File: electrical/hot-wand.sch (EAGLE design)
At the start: 186 parts, among them IC1 12V R-78K12-2.0, IC2 3V3 R-78K3.3, Q1 STP19NF20, Q2 IRF510, Q3 BC846B, Q4 SIRS5800DP-T1-GE3, Q5 2N7002K, Q6 DMTH64M2LPDWQ-13, Q7 G3404, SW1 SW-TACT-SIDE, U1 TPS54560DDA, U2 1EDN8511BXUSA1, U3 INA138, U4 LM74700QDBVTQ1, U5 AP53781, U6 SSD1306-4PIN-0.91N-VERT, U7 STM32F030F4P6, Y1 27.12 MHz 10pF

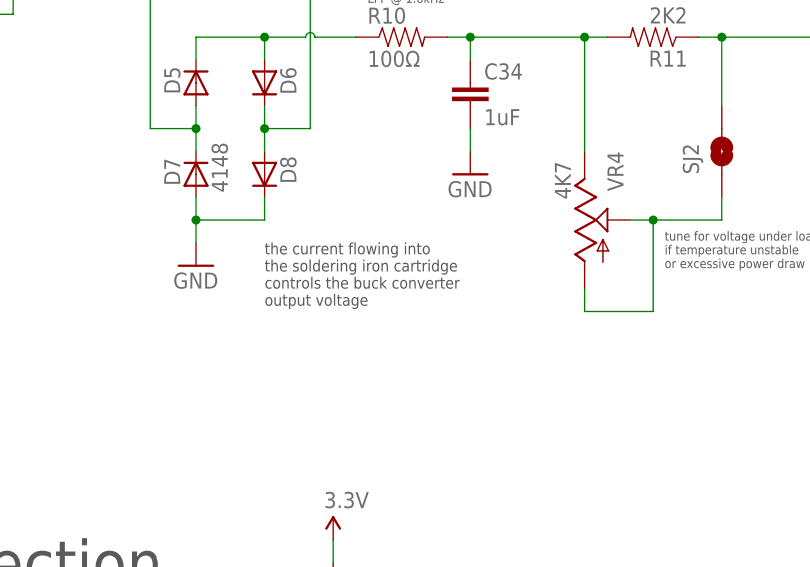
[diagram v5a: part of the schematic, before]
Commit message: 22 ohm resistor now 2W capable
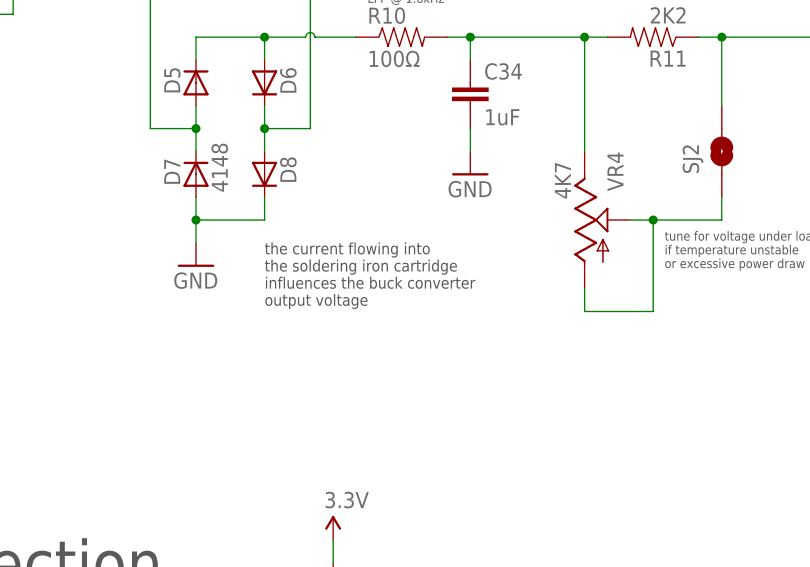
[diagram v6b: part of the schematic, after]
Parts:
- R21: device hot-wand:RESISTOR0603-RES -> hot-wand:RESISTOR2512; JLCPARTNUM C23345 -> C5204054
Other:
- note added: "the current flowing into the soldering iron cartridge influences the buck converter output voltage"
- note removed: "the current flowing into the soldering iron cartridge controls the buck converter output voltage"
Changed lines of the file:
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@@
 </part>
 <part name="GND13" library="hot-wand" deviceset="GND" device=""/>
-<part name="R21" library="hot-wand" deviceset="RESISTOR" device="0603-RES" value="22Ω">
-<attribute name="JLCPARTNUM" value="C23345"/>
+<part name="R21" library="hot-wand" deviceset="RESISTOR" device="2512" value="22Ω">
+<attribute name="JLCPARTNUM" value="C5204054"/>
 </part>
 <part name="L9" library="hot-wand" deviceset="L-US" device="TFI0410" value="22uH">
@@
 <text x="307.34" y="-187.96" size="1.27" layer="97" align="top-left">the current flowing into
 the soldering iron cartridge
-controls the buck converter
+influences the buck converter
 output voltage</text>
 <text x="254" y="-226.06" size="5.08" layer="97">Tip Detection</text>

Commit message: added another TVS diode to protect the buck converter
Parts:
- added TVS6: SMAJ22A, hot-wand:TVSSMA
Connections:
- net +24V: now also TVS6.2
- net GND: now also TVS6.1
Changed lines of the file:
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@@
 <part name="GND64" library="hot-wand" deviceset="GND" device=""/>
 <part name="JP5" library="hot-wand" deviceset="M06" device="LOCK"/>
+<part name="TVS6" library="hot-wand" deviceset="TVS" device="SMA" value="SMAJ22A">
+<attribute name="JLCPCBPART" value="C41376403"/>
+</part>
+<part name="GND63" library="hot-wand" deviceset="GND" device=""/>
 </parts>
 <sheets>
@@
 <instance part="GND64" gate="1" x="180.34" y="-703.58"/>
 <instance part="JP5" gate="G$1" x="187.96" y="-688.34" rot="R180"/>
+<instance part="TVS6" gate="G$1" x="259.08" y="-25.4" rot="R180">
+<attribute name="JLCPCBPART" x="259.08" y="-25.4" size="1.27" layer="96" rot="R180" display="off"/>
+</instance>
+<instance part="GND63" gate="1" x="264.16" y="-30.48"/>
 </instances>
 <busses>
@@
 <junction x="180.34" y="-693.42"/>
 <junction x="180.34" y="-688.34"/>
+</segment>
+<segment>
+<pinref part="TVS6" gate="G$1" pin="1"/>
+<pinref part="GND63" gate="1" pin="GND"/>
+<wire x1="261.62" y1="-25.4" x2="264.16" y2="-25.4" width="0.1524" layer="91"/>
+<wire x1="264.16" y1="-25.4" x2="264.16" y2="-27.94" width="0.1524" layer="91"/>
 </segment>
 </net>
@@
 <pinref part="R2" gate="G$1" pin="2"/>
 <wire x1="241.3" y1="-30.48" x2="243.84" y2="-30.48" width="0.1524" layer="91"/>
-<wire x1="243.84" y1="-30.48" x2="243.84" y2="-20.32" width="0.1524" layer="91"/>
+<wire x1="243.84" y1="-30.48" x2="243.84" y2="-25.4" width="0.1524" layer="91"/>
 <pinref part="R3" gate="G$1" pin="2"/>
+<wire x1="243.84" y1="-25.4" x2="243.84" y2="-20.32" width="0.1524" layer="91"/>
 <wire x1="241.3" y1="-40.64" x2="243.84" y2="-40.64" width="0.1524" layer="91"/>
 <wire x1="243.84" y1="-40.64" x2="243.84" y2="-30.48" width="0.1524" layer="91"/>
@@
 <junction x="243.84" y="-20.32"/>
 <junction x="243.84" y="-30.48"/>
-</segment>
-<segment>
+<pinref part="TVS6" gate="G$1" pin="2"/>
+<wire x1="254" y1="-25.4" x2="243.84" y2="-25.4" width="0.1524" layer="91"/>
+<junction x="243.84" y="-25.4"/>
+</segment>
+<segment>

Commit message: added out-to-in diode for buck converter
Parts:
- added D13: 2A 60V, hot-wand:DIODE-SCHOTTKYSOD123FL
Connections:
- net DC-IN: now also D13.C
- net N$23: now also D13.A
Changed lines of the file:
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@@
 </part>
 <part name="GND63" library="hot-wand" deviceset="GND" device=""/>
+<part name="D13" library="hot-wand" deviceset="DIODE-SCHOTTKY" device="SOD123FL" value="2A 60V">
+<attribute name="JLCPARTNUM" value="C53340922"/>
+<attribute name="PARTNUM" value="STPS2L60ZFY"/>
+</part>
 </parts>
 <sheets>
@@
 0.547V/A
 6.04A max</text>
-<text x="68.58" y="-10.16" size="5.08" layer="97">Main Power Buck Converter</text>
+<text x="68.58" y="-2.54" size="5.08" layer="97">Main Power Buck Converter</text>
 <text x="101.6" y="-502.92" size="5.08" layer="97">Power Sensing</text>
 <text x="43.18" y="-279.4" size="5.08" layer="97">RF Amp Gate Driver</text>
@@
 </instance>
 <instance part="GND63" gate="1" x="264.16" y="-30.48"/>
+<instance part="D13" gate="G$1" x="114.3" y="-10.16" rot="R180">
+<attribute name="JLCPARTNUM" x="114.3" y="-10.16" size="1.27" layer="96" rot="R180" display="off"/>
+<attribute name="PARTNUM" x="114.3" y="-10.16" size="1.27" layer="96" rot="R180" display="off"/>
+</instance>
 </instances>
 <busses>
@@
 <wire x1="60.96" y1="-20.32" x2="63.5" y2="-20.32" width="0.1524" layer="91"/>
 <wire x1="63.5" y1="-20.32" x2="73.66" y2="-20.32" width="0.1524" layer="91"/>
-<wire x1="73.66" y1="-20.32" x2="91.44" y2="-20.32" width="0.1524" layer="91"/>
+<wire x1="73.66" y1="-20.32" x2="86.36" y2="-20.32" width="0.1524" layer="91"/>
+<wire x1="86.36" y1="-20.32" x2="91.44" y2="-20.32" width="0.1524" layer="91"/>
 <wire x1="60.96" y1="-20.32" x2="60.96" y2="-12.7" width="0.1524" layer="91"/>
 <wire x1="60.96" y1="-12.7" x2="55.88" y2="-12.7" width="0.1524" layer="91"/>
@@
 <junction x="73.66" y="-20.32"/>
 <pinref part="F1" gate="G$1" pin="2"/>
+<pinref part="D13" gate="G$1" pin="C"/>
+<wire x1="111.76" y1="-10.16" x2="86.36" y2="-10.16" width="0.1524" layer="91"/>
+<wire x1="86.36" y1="-10.16" x2="86.36" y2="-20.32" width="0.1524" layer="91"/>
+<junction x="86.36" y="-20.32"/>
 </segment>
 <segment>
@@
 <wire x1="127" y1="-27.94" x2="139.7" y2="-27.94" width="0.1524" layer="91"/>
 <wire x1="139.7" y1="-27.94" x2="139.7" y2="-20.32" width="0.1524" layer="91"/>
-<wire x1="139.7" y1="-20.32" x2="144.78" y2="-20.32" width="0.1524" layer="91"/>
+<wire x1="139.7" y1="-20.32" x2="142.24" y2="-20.32" width="0.1524" layer="91"/>
 <pinref part="C1" gate="G$1" pin="2"/>
+<wire x1="142.24" y1="-20.32" x2="144.78" y2="-20.32" width="0.1524" layer="91"/>
 <wire x1="137.16" y1="-20.32" x2="139.7" y2="-20.32" width="0.1524" layer="91"/>
 <pinref part="D1" gate="G$1" pin="C"/>
@@
 <junction x="139.7" y="-20.32"/>
 <pinref part="L1" gate="G$1" pin="1"/>
-</segment>
-</net>
+<pinref part="D13" gate="G$1" pin="A"/>
+<wire x1="116.84" y1="-10.16" x2="142.24" y2="-10.16" width="0.1524" layer="91"/>
+<wire x1="142.24" y1="-10.16" x2="142.24" y2="-20.32" width="0.1524" layer="91"/>
+<junction x="142.24" y="-20.32"/>
+</segment>
+</net>
